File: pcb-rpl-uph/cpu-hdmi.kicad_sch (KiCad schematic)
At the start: 1 part, among them U5 RPL_UPH_FCBGA1744

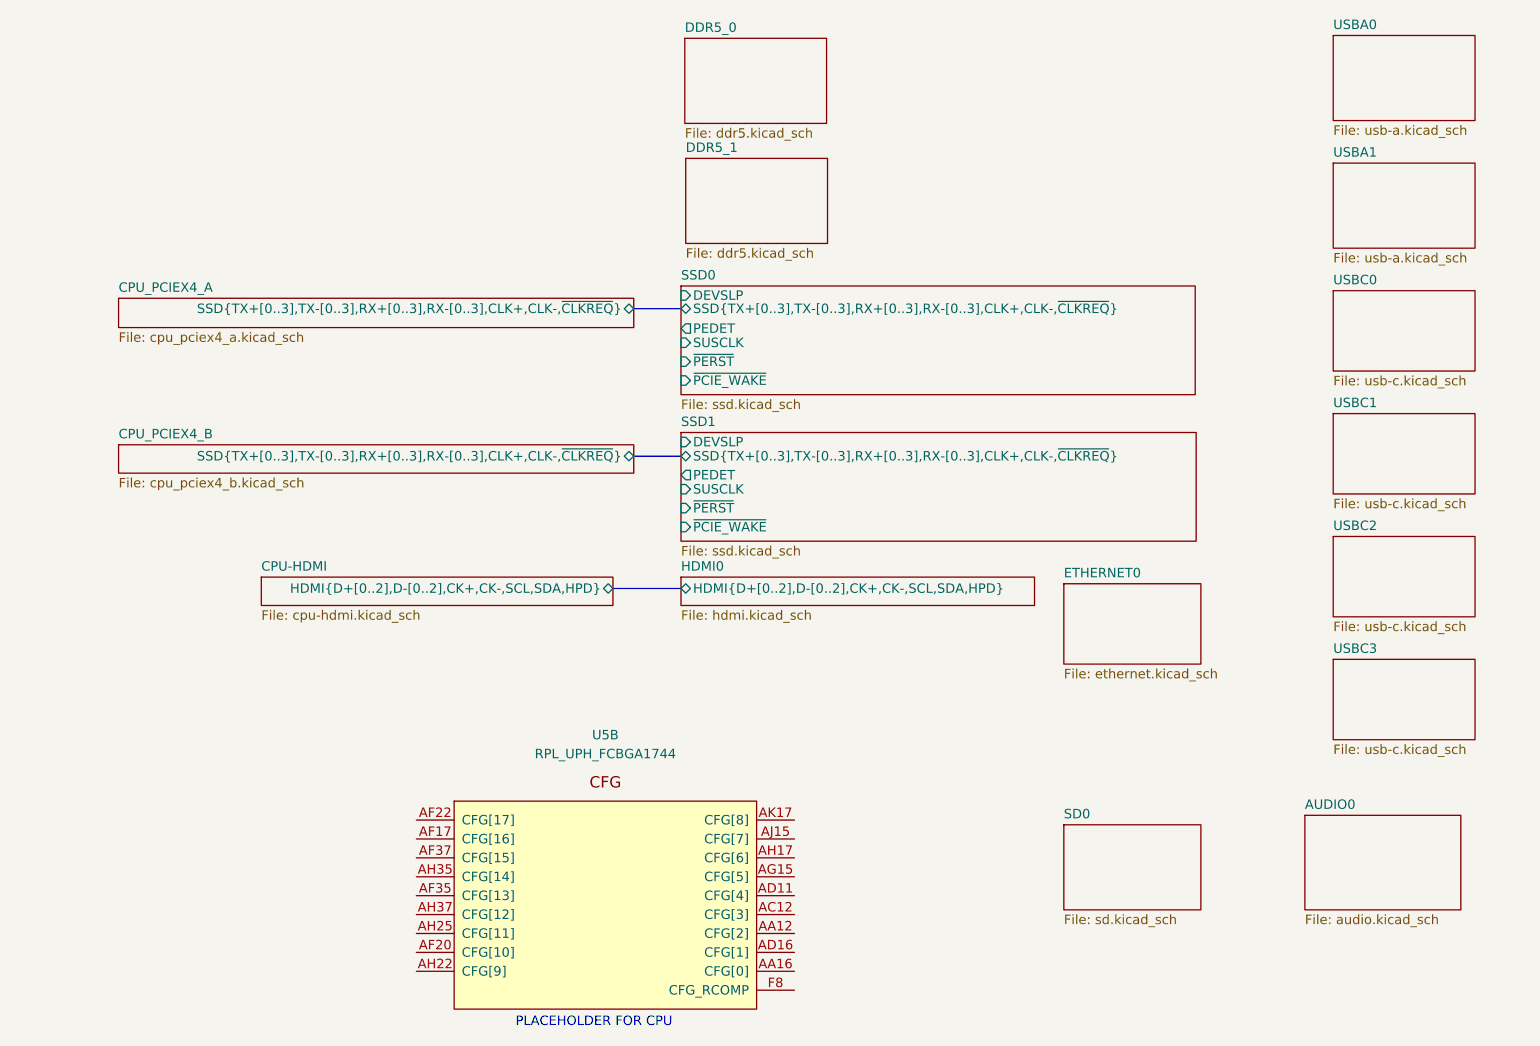
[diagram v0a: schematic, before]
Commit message: Connect CPU HDMI to port
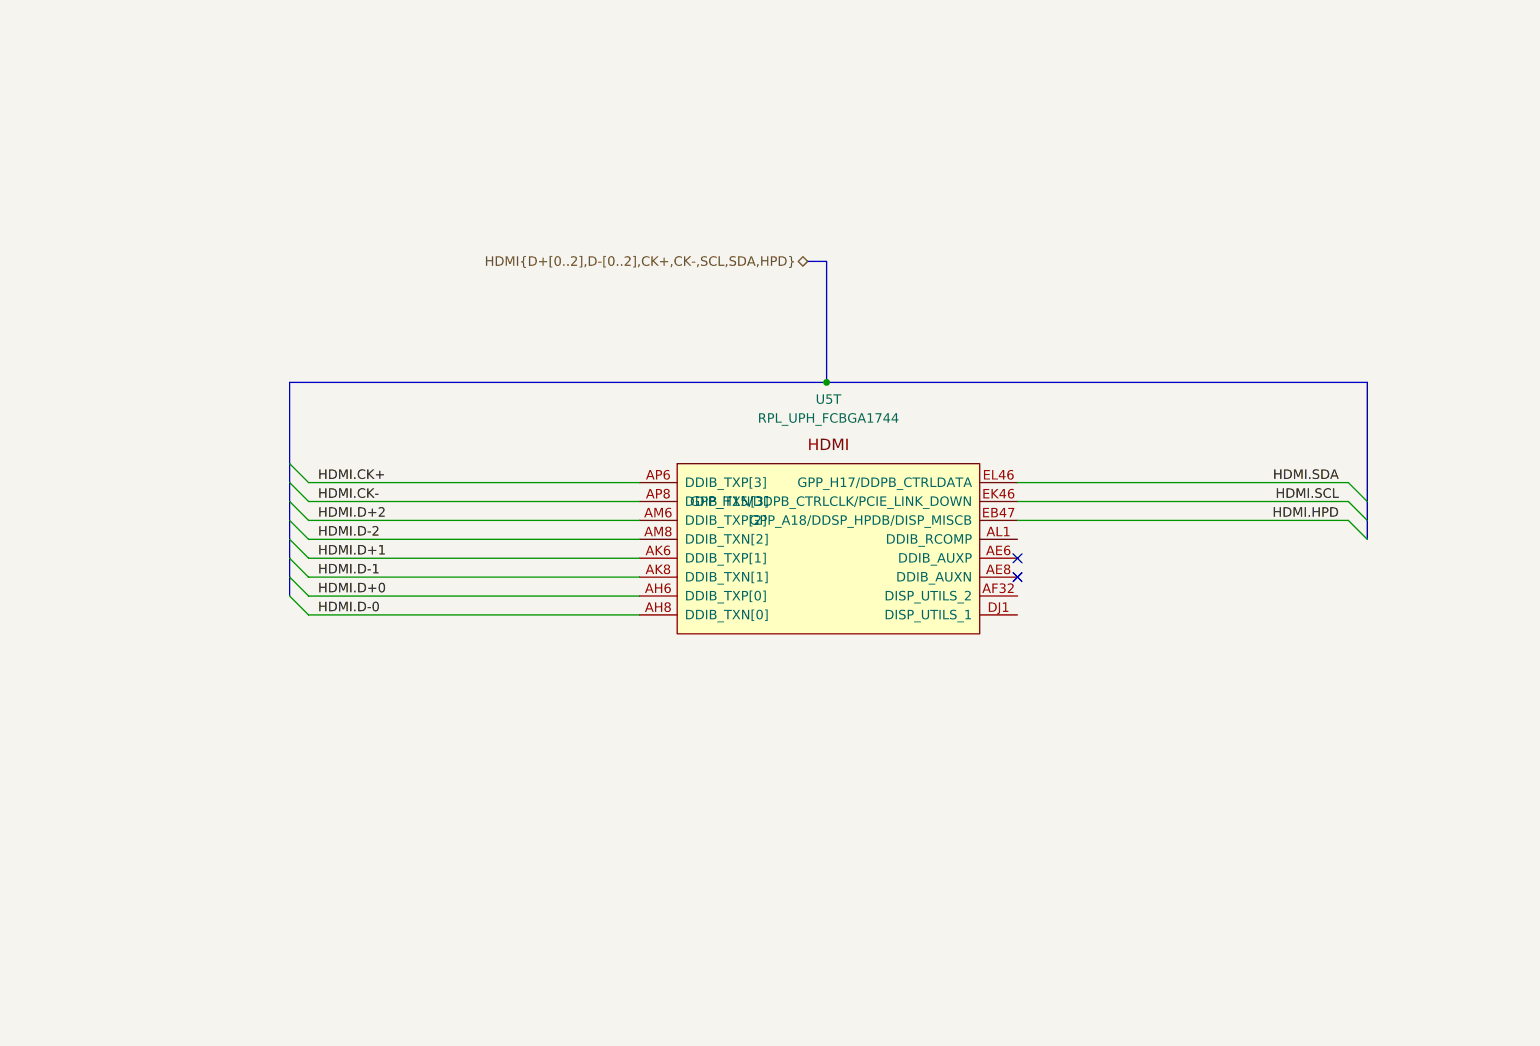
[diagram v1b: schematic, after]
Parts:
- removed U5: RPL_UPH_FCBGA1744, local:RPL_UPH_FCBGA1744, symbol local:RPL_UPH_FCBGA1744
- added U5: RPL_UPH_FCBGA1744, symbol local:RPL_UPH_FCBGA1744
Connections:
- new net HDMI.CK+: U5.AP6 (DDIB_TXP[3])
- new net HDMI.CK-: U5.AP8 (DDIB_TXN[3])
- new net HDMI.D+0: U5.AH6 (DDIB_TXP[0])
- new net HDMI.D+1: U5.AK6 (DDIB_TXP[1])
- new net HDMI.D+2: U5.AM6 (DDIB_TXP[2])
- new net HDMI.D-0: U5.AH8 (DDIB_TXN[0])
- new net HDMI.D-1: U5.AK8 (DDIB_TXN[1])
- new net HDMI.D-2: U5.AM8 (DDIB_TXN[2])
- new net HDMI.HPD: U5.EB47 (GPP_A18/DDSP_HPDB/DISP_MISCB)
- new net HDMI.SCL: U5.EK46 (GPP_H15/DDPB_CTRLCLK/PCIE_LINK_DOWN)
- new net HDMI.SDA: U5.EL46 (GPP_H17/DDPB_CTRLDATA)
- no-connect marks 0 -> 2
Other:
- removed sheet AUDIO0
- removed sheet CPU-HDMI
- removed sheet CPU_PCIEX4_A
- removed sheet CPU_PCIEX4_B
- removed sheet DDR5_0
- removed sheet DDR5_1
- removed sheet ETHERNET0
- removed sheet HDMI0
- removed sheet SD0
- removed sheet SSD0
- removed sheet SSD1
- removed sheet USBA0
- removed sheet USBA1
- removed sheet USBC0
- removed sheet USBC1
- removed sheet USBC2
- removed sheet USBC3
- note removed: "PLACEHOLDER FOR CPU"
